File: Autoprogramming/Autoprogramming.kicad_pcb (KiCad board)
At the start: 2 copper layers, 8 parts, among them Q1 S8050 J3Y 200-350, Q2 S8050 J3Y 200-350

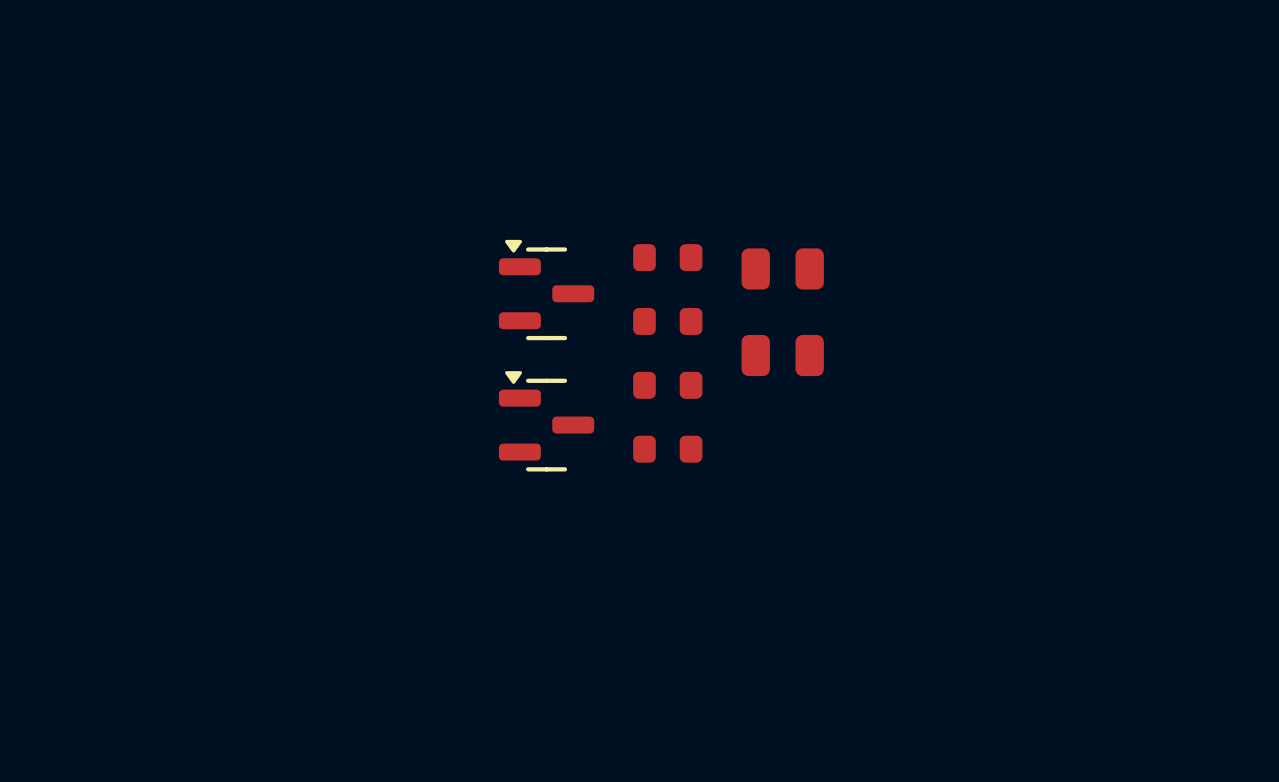
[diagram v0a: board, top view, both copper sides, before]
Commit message: electronics: Sync latest designs from working directory
- Rename Puck board files (was Vent.kicad_* → Puck.kicad_*)
- Add full Comps libraries (footprints, models, symbols) for all four boards
- Add manufacturing-current/ Gerber outputs and renders for all boards
- Add new components: ESP32-C6-MINI-1 (Puck), ESP32-H2-MINI-1 (Vent), NCU15XH103F60RC (BMS)
- Add PCM JLCPCB passive symbol libraries across all boards
- Add per-project .gitignore files and Autoprogramming/AUTOPROGRAMMING_REVIEW.md
- Add root-level BOM files, sourcing audit, and manufacturing readiness ledger
- Update KiCad design files and Gerbers for BMS, Autoprogramming, and Vent

Co-Authored-By: Claude Sonnet 4.6 <noreply@anthropic.com>

Original-author: Zachariah K. Sharma <zachariah.sharma@gmail.com>
Source-commit: 261c676a3a26a8c60302274465dd756769088335
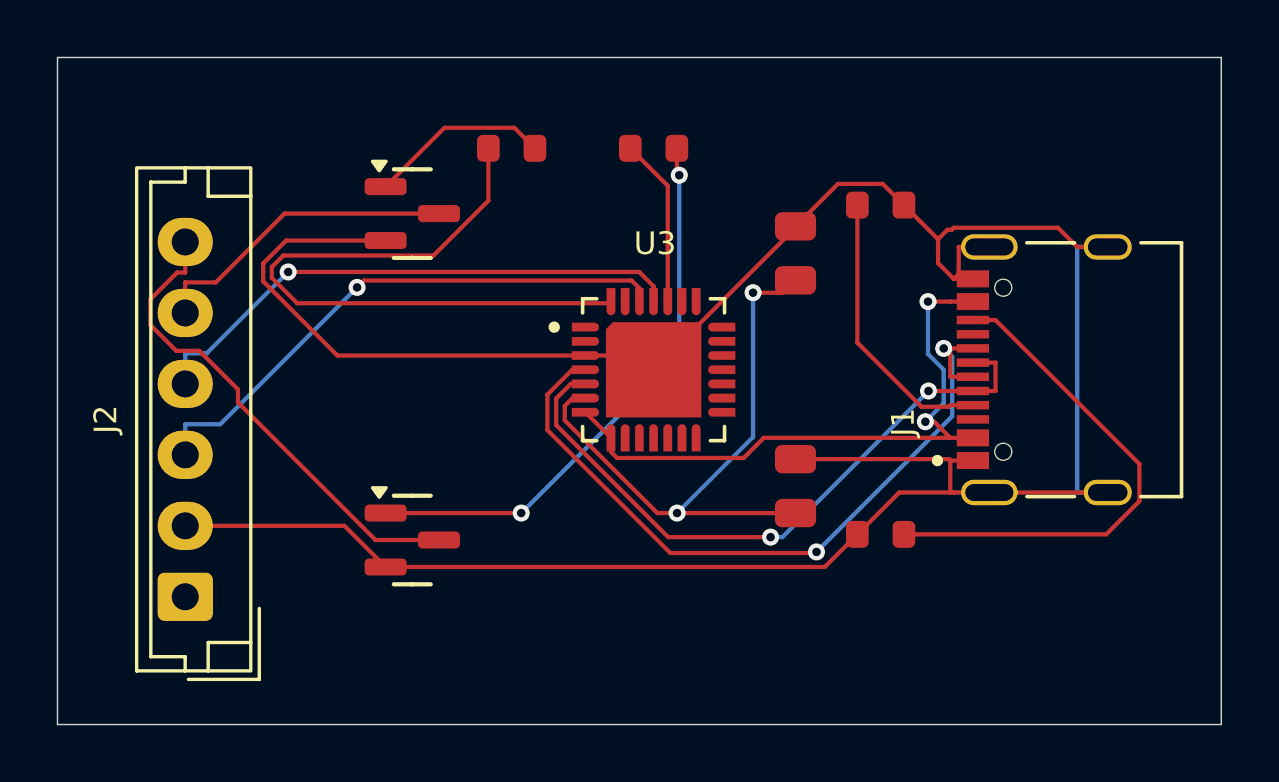
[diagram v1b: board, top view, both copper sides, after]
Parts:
- added J1: TYPE-C-31-M-12, Footprints:HRO_TYPE-C-31-M-12, F.Cu at (185.0, 91.0)
- added J2: Conn_01x06_Pin, Footprints:JST_EH_B6B-EH-A_1x06_P2.50mm_Vertical, F.Cu at (152.5, 99.0)
- added U3: CP2102N-A02-GQFN28R, Footprints:IC_CP2102N-A02-GQFN28R, F.Cu at (169.0, 91.0)
- C1: footprint PCM_JLCPCB:C_0805 -> PCM_JLCPCB:C_0805_100nF
- C2: footprint PCM_JLCPCB:C_0805 -> PCM_JLCPCB:C_0805_4u7
- moved R6 11.9 mm to (164.0, 83.2)
- moved R4 10.6 mm to (177.0, 96.8)
- moved R5 8.36 mm to (169.0, 83.2)
- moved R3 7.72 mm to (177.0, 85.2)
- moved Q2 6.23 mm to (160.5, 97.0)
- moved Q1 5.51 mm to (160.5, 85.5)
- moved C2 4.62 mm to (174.0, 95.1), turned to 90 degrees
- moved C1 0.71 mm to (174.0, 86.9), turned to 90 degrees
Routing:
- net GND: track 0.00 -> 97.4 mm
- net USB_D+: track 0.00 -> 26.3 mm, vias 0 -> 2
- net USB_D-: track 0.00 -> 23.2 mm, vias 0 -> 2
- net DTR: track 0.00 -> 23.2 mm
- net VBUS: track 0.00 -> 22.3 mm, vias 0 -> 2
- net Net-(U3-VDD): track 0.00 -> 21.4 mm, vias 0 -> 2
- net Net-(Q2-B): track 0.00 -> 20.0 mm, vias 0 -> 2
- net RXD0: track 0.00 -> 19.8 mm, vias 0 -> 1
- net TXD0: track 0.00 -> 19.5 mm, vias 0 -> 1
- net Net-(J1-CC2): track 0.00 -> 18.1 mm
- net IO0: track 0.00 -> 17.2 mm
- net EN: track 0.00 -> 11.0 mm
- net Net-(J1-CC1): track 0.00 -> 9.87 mm
- net Net-(Q1-B): track 0.00 -> 6.42 mm
- net RTS: track 0.00 -> 5.95 mm
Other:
- board outline added: 41 x 23.5 mm

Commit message: electronics: Trace optimization and GND pour additions via KiCad MCP review
- All 4 boards: set minTrackWidth = 0.10 mm so DRC enforces a fab-safe floor
- Autoprogramming: add full-board GND pours on F.Cu and B.Cu (board had no
  copper pours; pours improve USB return-path noise immunity)
- Puck: add full-board B.Cu GND pour (existing B.Cu zone was tiny and unfilled)
- BMS/Vent: GND pours already present on both layers, no zone changes needed

DRC results post-changes:
- BMS: 0 violations
- Autoprogramming: 0 violations
- Vent: 0 violations
- Puck: 25 pre-existing violations surfaced (12 drill_out_of_range for 0.2 mm
  ESP32-C6 GND-pad stitching vias below JLCPCB 0.3 mm standard minimum; 4
  solder_mask_bridge at spring-contact pads; misc silk/edge warnings) — these
  were present before this session and are documented in the manufacturing notes

Co-Authored-By: Claude Sonnet 4.6 <noreply@anthropic.com>

Original-author: Zachariah K. Sharma <zachariah.sharma@gmail.com>
Source-commit: 734f09ef7afe0818f883ddc77e1c44a372e9487f
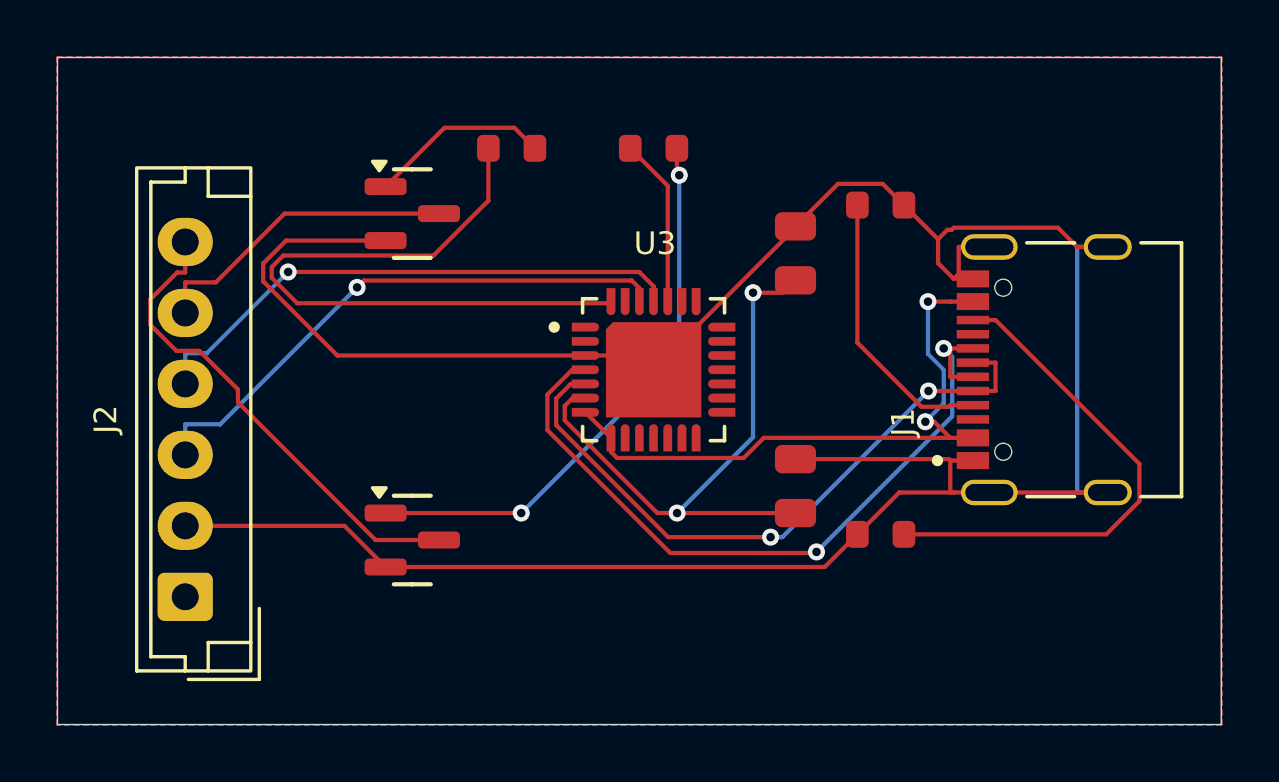
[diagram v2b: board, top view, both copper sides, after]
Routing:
- added copper zone on B.Cu, net GND
- added copper zone on F.Cu, net GND
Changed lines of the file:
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@@
 		(net 15)
+	)
+	(zone
+		(net 2)
+		(net_name "GND")
+		(layer "F.Cu")
+		(hatch edge 0.5)
+		(connect_pads
+			(clearance 0.3)
+		)
+		(min_thickness 0.2)
+		(filled_areas_thickness no)
+		(fill yes
+			(thermal_gap 0.5)
+			(thermal_bridge_width 0.5)
+		)
+		(polygon
+			(pts
+				(xy 147.975 79.975) (xy 189.025 79.975) (xy 189.025 103.525) (xy 147.975 103.525)
+			)
+		)
+	)
+	(zone
+		(net 2)
+		(net_name "GND")
+		(layer "B.Cu")
+		(hatch edge 0.5)
+		(connect_pads
+			(clearance 0.3)
+		)
+		(min_thickness 0.2)
+		(filled_areas_thickness no)
+		(fill yes
+			(thermal_gap 0.5)
+			(thermal_bridge_width 0.5)
+		)
+		(polygon
+			(pts
+				(xy 147.975 79.975) (xy 189.025 79.975) (xy 189.025 103.525) (xy 147.975 103.525)
+			)
+		)
 	)
 	(embedded_fonts no)
